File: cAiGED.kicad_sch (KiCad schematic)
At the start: 0 parts

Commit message: Updated project files
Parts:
- added IC1: STM32N657X0H3Q, BGA264C80P17X17_1400X1400X100, symbol SamacSys_Parts3:STM32N657X0H3Q

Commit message: Updated Documentation files. Updated MCU symbol
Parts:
- added unit 2 of IC1

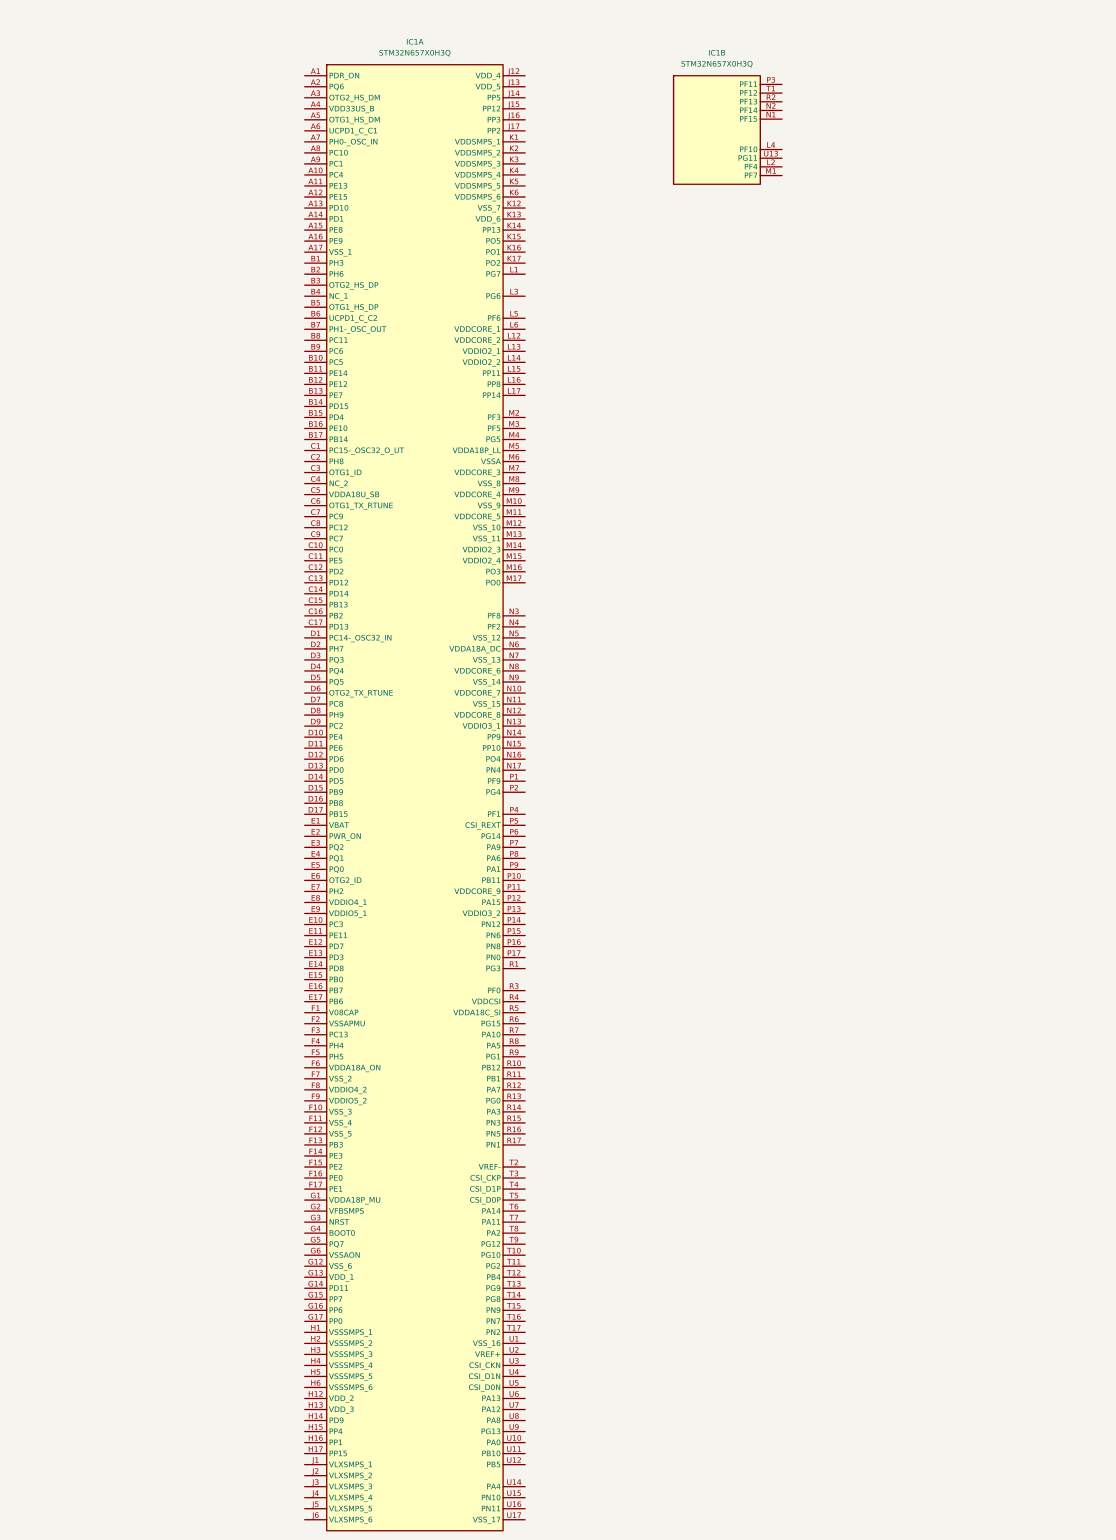
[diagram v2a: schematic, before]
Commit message: Updated MCU symbol
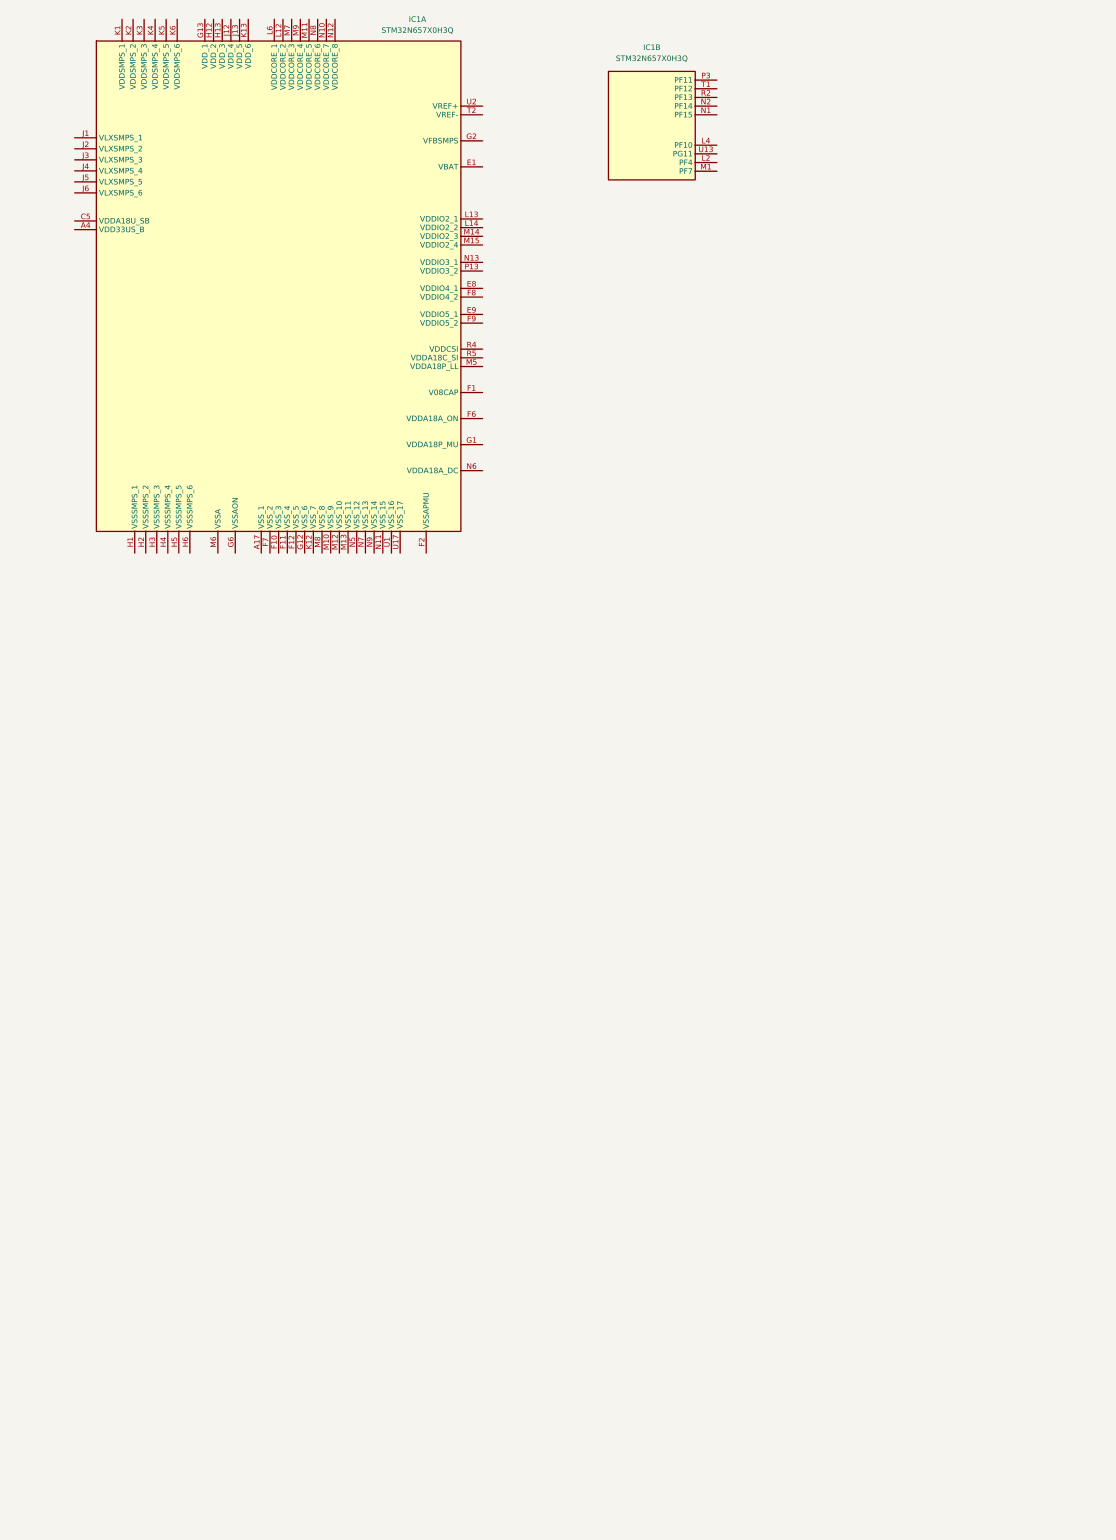
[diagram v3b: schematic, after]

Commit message: Updated MCU symbol - MCU Debug
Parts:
- added unit 3 of IC1

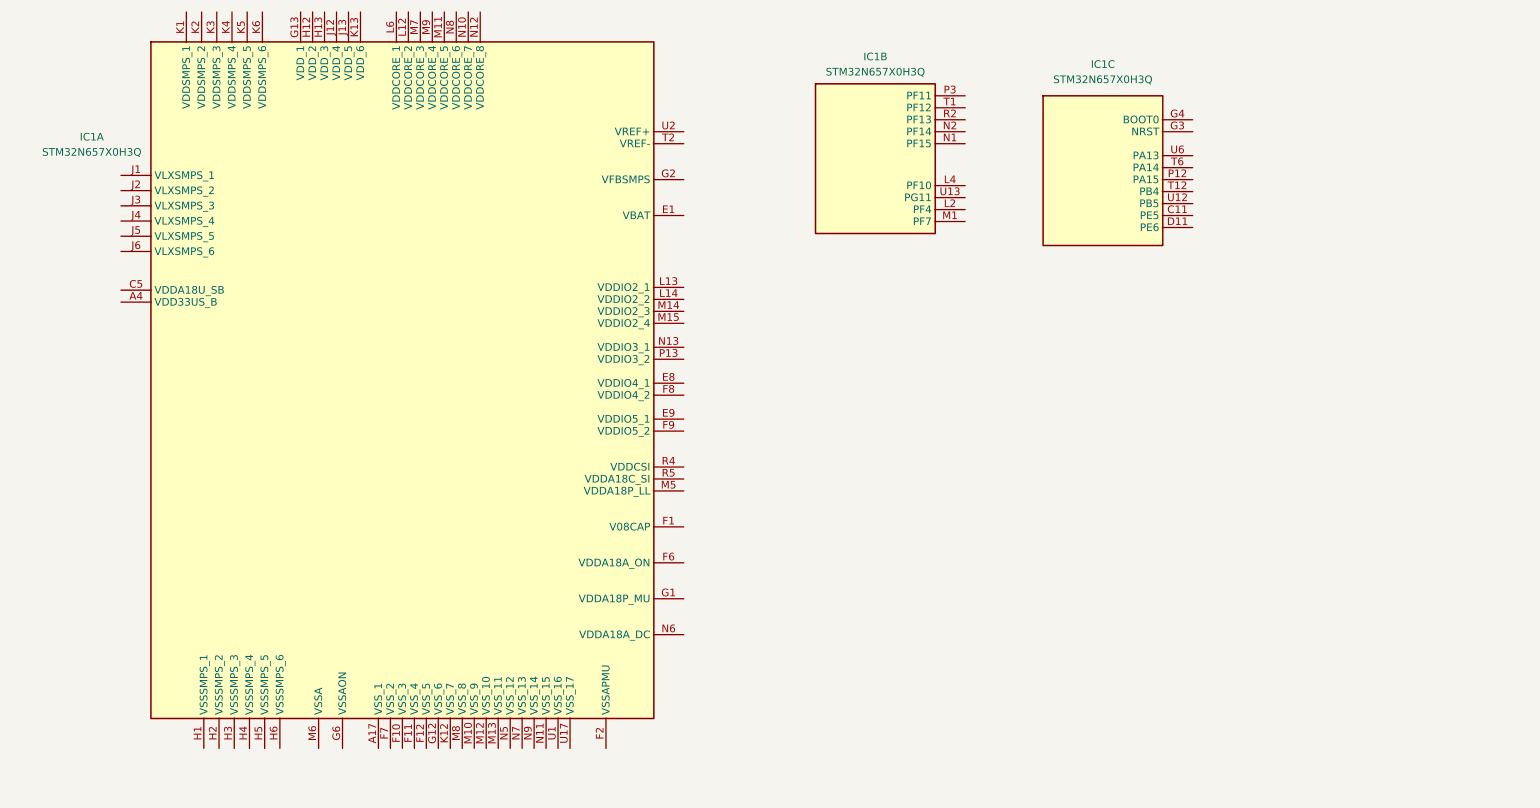
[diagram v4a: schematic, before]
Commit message: Updated MCU symbol - MCU USB
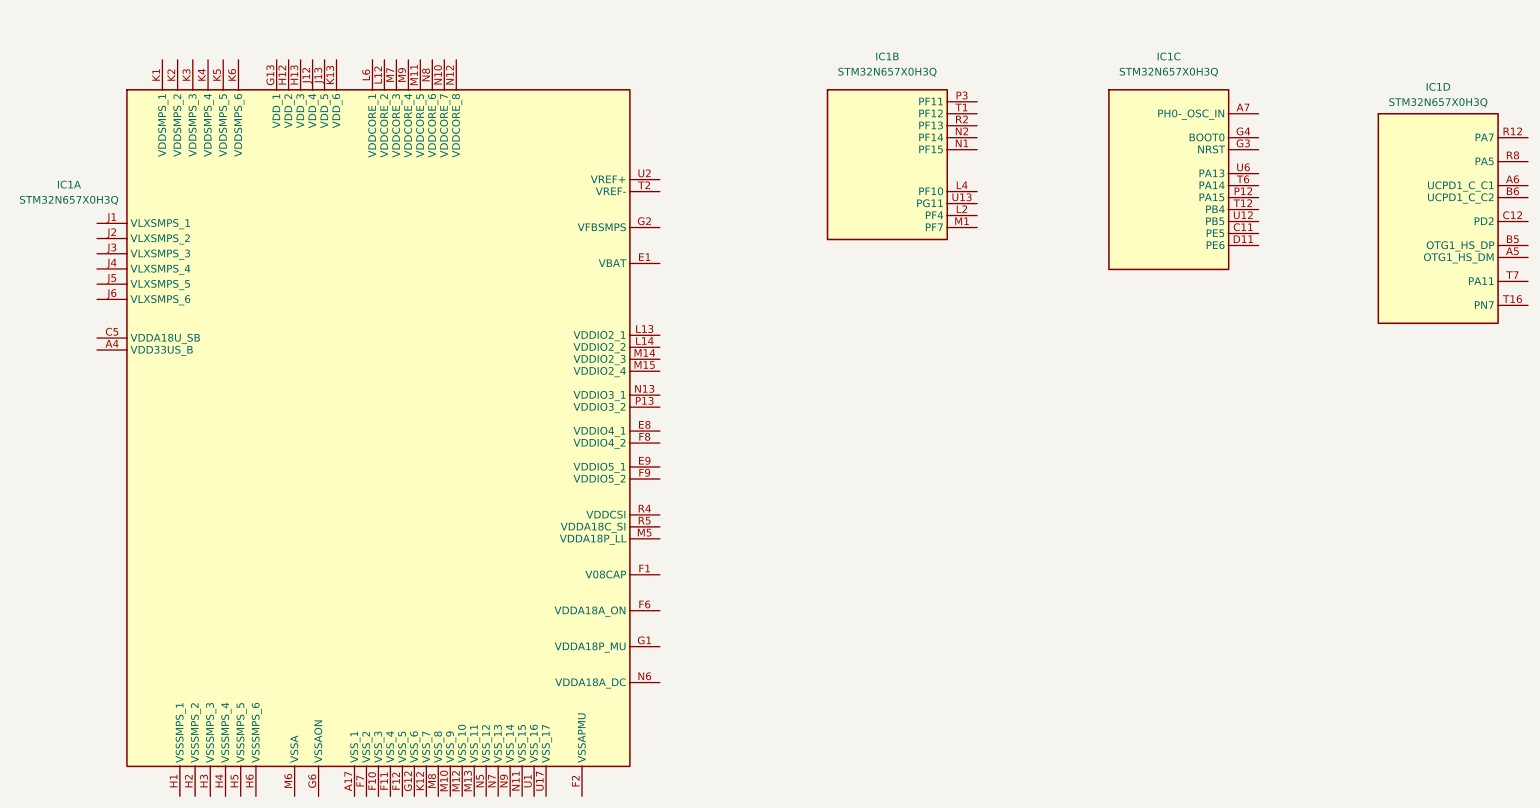
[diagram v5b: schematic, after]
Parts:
- added unit 4 of IC1
